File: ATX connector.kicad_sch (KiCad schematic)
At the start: 15 parts, among them J400 15246040, J402 ATX-24

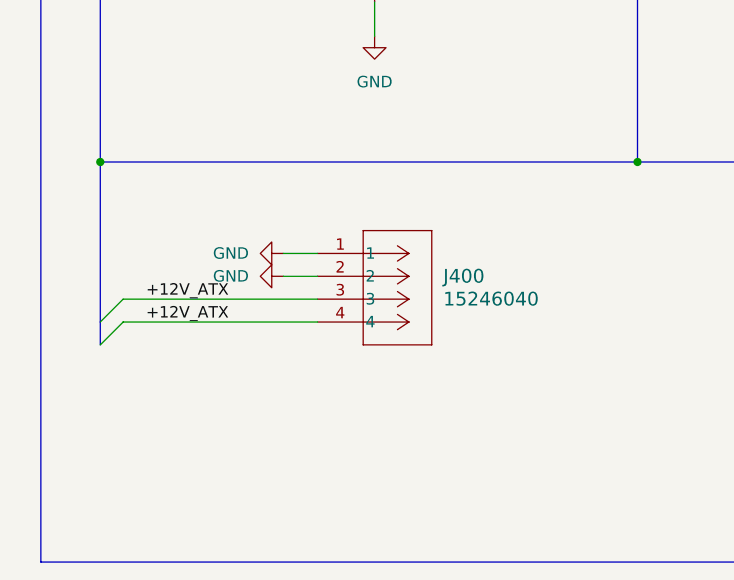
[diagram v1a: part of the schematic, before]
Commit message: add 2x6pin PCIe molex + PCBA to check
should work now
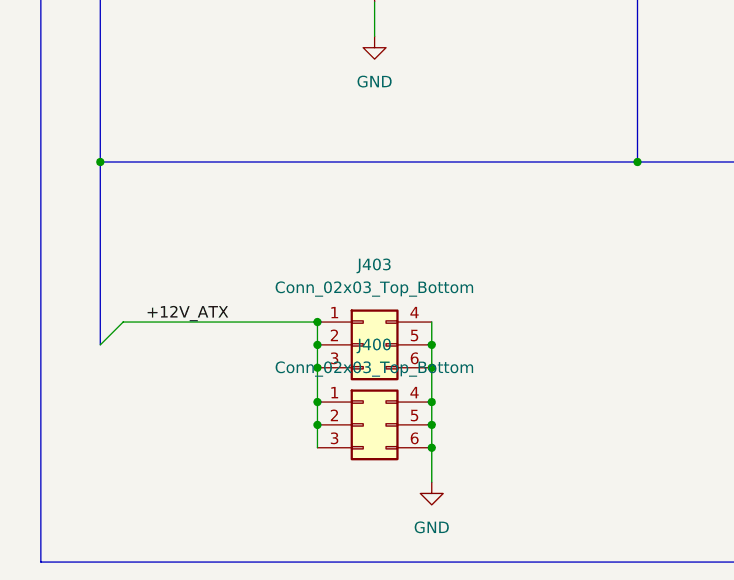
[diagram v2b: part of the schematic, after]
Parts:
- removed J400: 15246040, footprints:CONN_SDA-42404_04_MOL, symbol 2025-11-30_18-16-43:15246040
- added J400, J403: Conn_02x03_Top_Bottom, Connector_Molex:Molex_Mini-Fit_Jr_5569-06A2_2x03_P4.20mm_Horizontal, symbol Connector_Generic:Conn_02x03_Top_Bottom
- J402: footprint Connector_Molex:Molex_Mini-Fit_Jr_5566-24A2_2x12_P4.20mm_Vertical -> Connector_Molex:Molex_Mini-Fit_Jr_5566-24A_2x12_P4.20mm_Vertical
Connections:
- net +12V_ATX: now also J400.1 (Pin_1), J400.2 (Pin_2), J400.3 (Pin_3), J403.1 (Pin_1), J403.2 (Pin_2), J403.3 (Pin_3)
- net GND: now also J400.4 (Pin_4), J400.5 (Pin_5), J400.6 (Pin_6), J403.4 (Pin_4), J403.5 (Pin_5), J403.6 (Pin_6)

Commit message: generated final gerber
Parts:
- added J404: ATX-24, Connector_Molex:Molex_Mini-Fit_Jr_5569-24A2_2x12_P4.20mm_Horizontal, symbol Connector:ATX-24
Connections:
- new net: J404.1 (+3.3V), J404.12 (+3.3V), J404.13 (+3.3V), J404.2 (+3.3V)
- new net: J404.10 (+12V), J404.11 (+12V)
- new net: J404.15 (GND), J404.17 (GND), J404.18 (GND), J404.19 (GND), J404.24 (GND), J404.3 (GND), J404.5 (GND), J404.7 (GND)
- new net: J404.21 (+5V), J404.22 (+5V), J404.23 (+5V), J404.4 (+5V), J404.6 (+5V)
